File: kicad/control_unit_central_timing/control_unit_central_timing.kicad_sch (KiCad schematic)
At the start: 10 parts

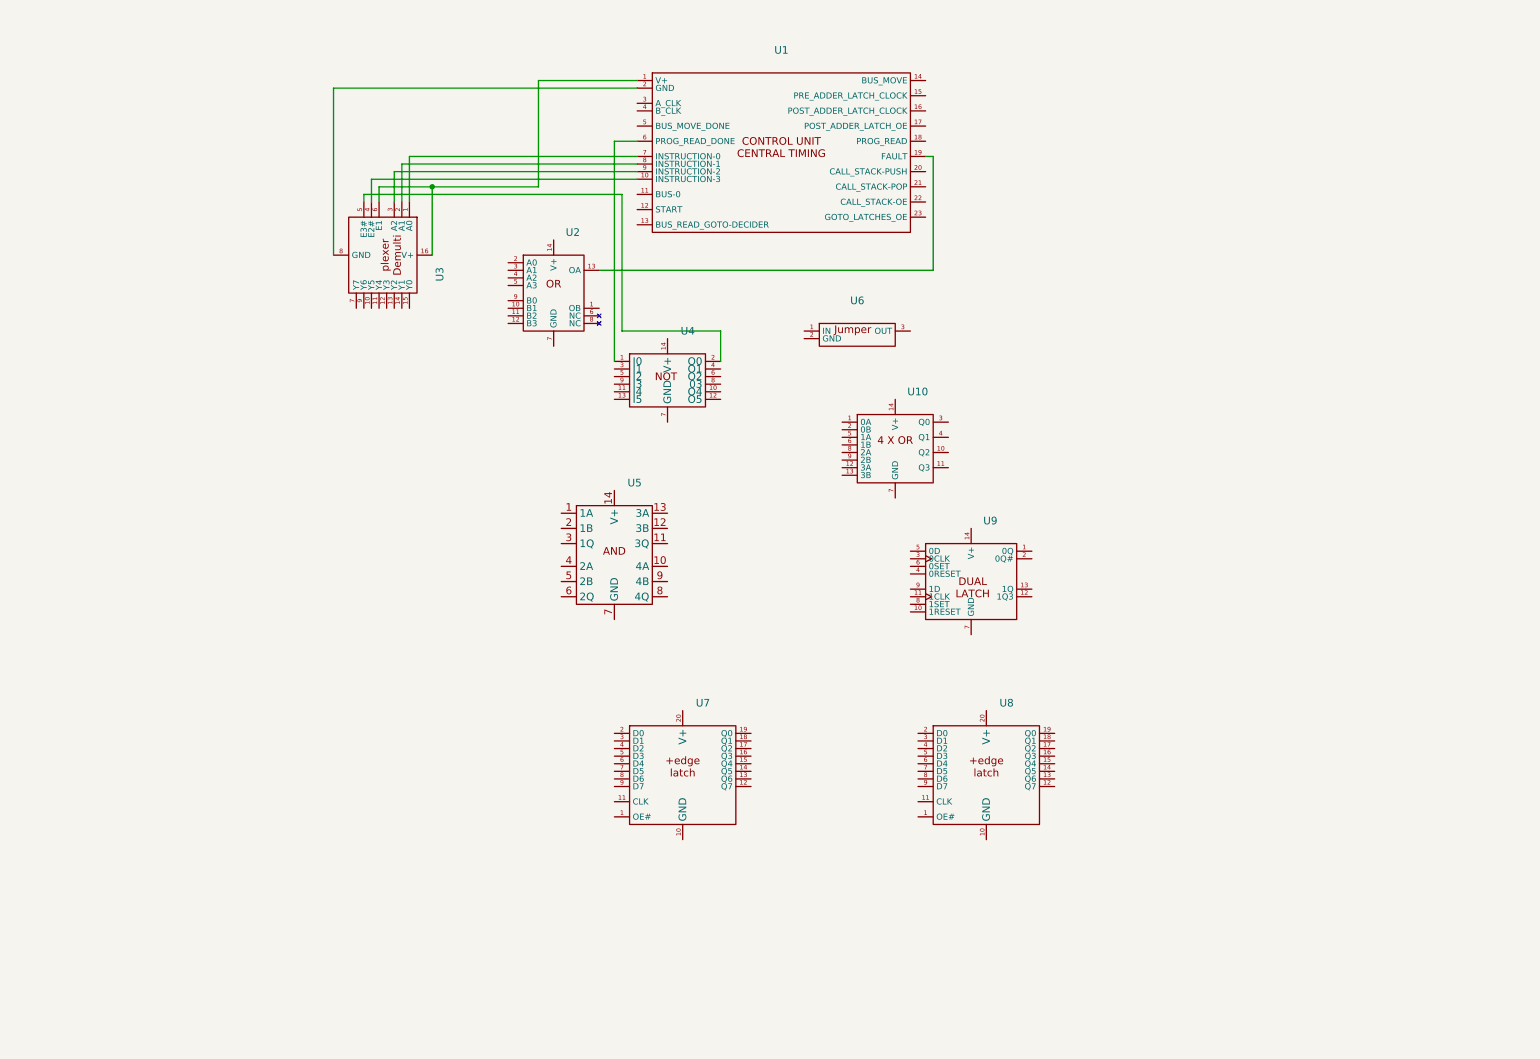
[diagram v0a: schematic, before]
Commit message: Working on control unit schematic
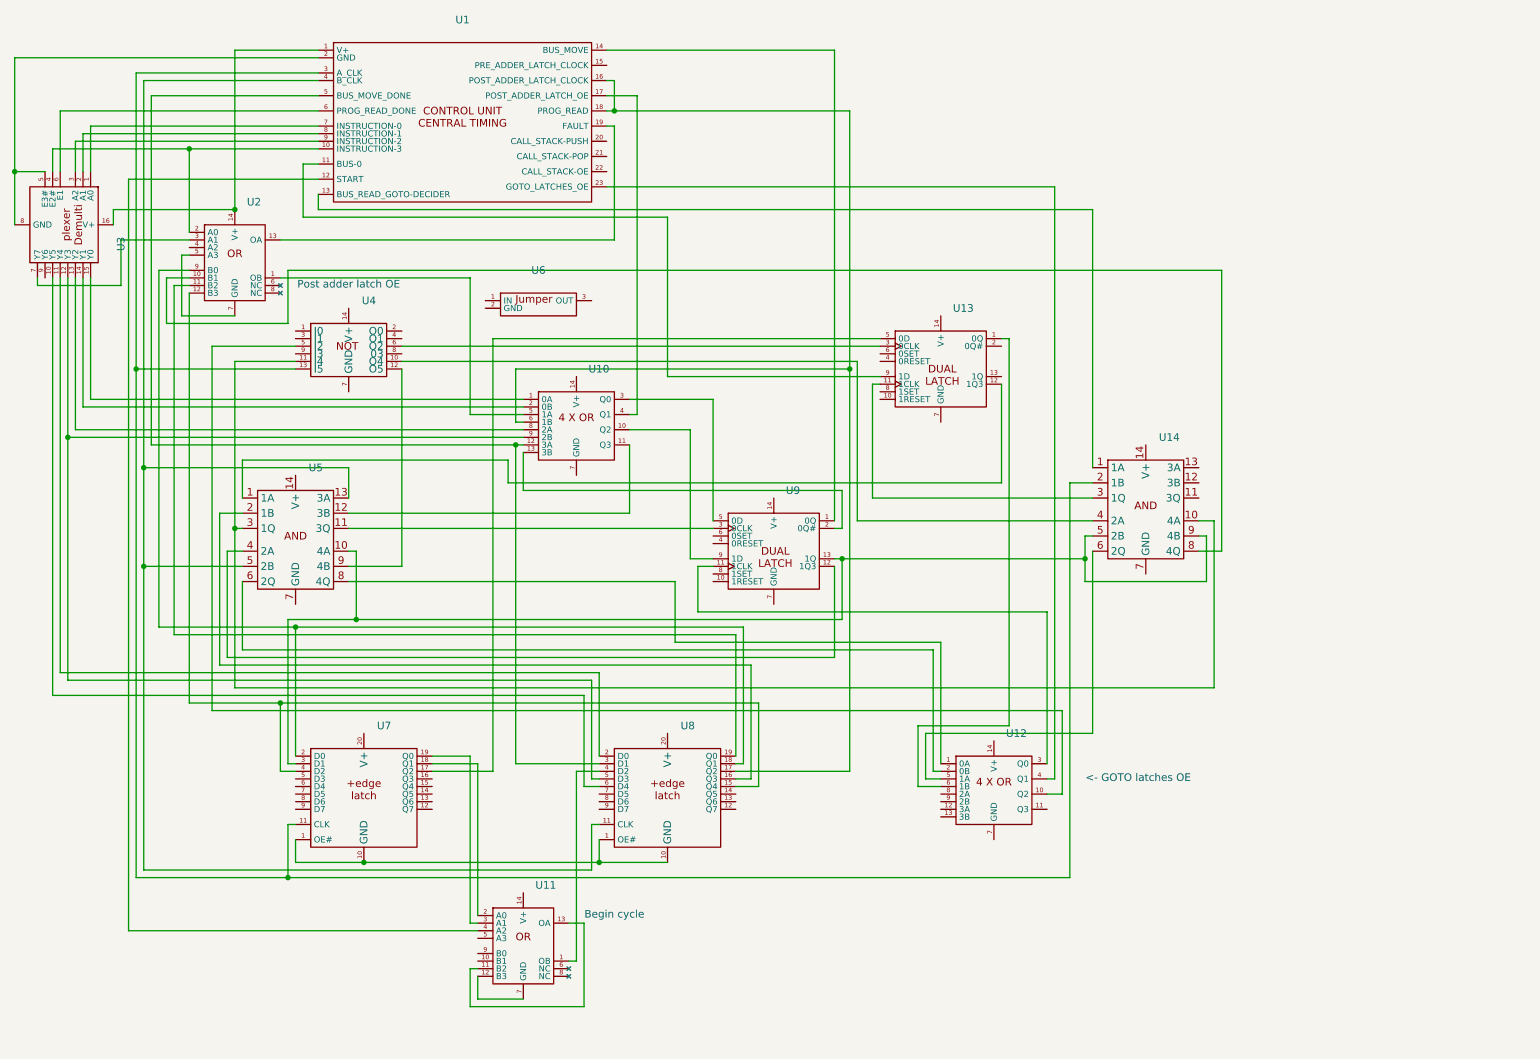
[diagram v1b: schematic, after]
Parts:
- added U11: ~, Package_DIP:DIP-14_W7.62mm, symbol custom_symbol_lib:dual_4_input_OR
- added U12: ~, Package_DIP:DIP-14_W7.62mm, symbol custom_symbol_lib:quad_OR
- added U13: ~, Package_DIP:DIP-14_W7.62mm, symbol custom_symbol_lib:dual_latch
- added U14: ~, Package_DIP:DIP-14_W7.62mm, symbol custom_symbol_lib:quad_and
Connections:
- net at U9.1 (0Q): now also U1.14 (BUS_MOVE)
- net at U9.11 (1CLK): now also U12.3 (Q0)
- net at U9.12 (1Q3): now also U5.4 (2A)
- net at U9.13 (1Q): now also U5.10 (4A), U7.3 (D1), U14.5 (2B), U14.9 (4B)
- net at U9.2 (0Q#): now also U10.13 (3B)
- net at U9.3 (0CLK): now also U5.11 (3Q)
- net at U9.5 (0D): now also U10.3 (Q0)
- net at U9.9 (1D): now also U10.10 (Q2)
- net at U8.1 (OE#): now also U7.1 (OE#), U7.10 (GND), U8.10 (GND)
- net at U8.11 (CLK): now also U1.4 (B_CLK), U5.13 (3A), U5.5 (2B)
- net at U8.15 (Q4): now also U2.12 (B3), U7.4 (D2)
- net at U8.16 (Q3): now also U5.2 (1B)
- net at U8.17 (Q2): now also U1.16 (POST_ADDER_LATCH_CLOCK), U1.18 (PROG_READ), U10.6 (1B)
- net at U8.18 (Q1): now also U2.9 (B0), U7.2 (D0)
- net at U8.19 (Q0): now also U2.11 (B2)
- net at U8.2 (D0): now also U3.11 (Y4)
- net at U8.3 (D1): now also U1.5 (BUS_MOVE_DONE), U10.12 (3A)
- net at U8.4 (D2): now also U11.1 (OB)
- net at U8.5 (D3): now also U10.9 (2B), U3.12 (Y3)
- net at U8.6 (D4): now also U3.10 (Y5)
- net at U5.1 (1A): now also U13.12 (1Q3)
- net at U5.12 (3B): now also U10.11 (Q3)
- net at U5.3 (1Q): now also U4.11 (I4), U14.10 (4A)
- net at U5.6 (2Q): now also U12.2 (0B)
- net at U5.8 (4Q): now also U12.1 (0A)
- net at U5.9 (4B): now also U4.12 (O5)
- net at U7.11 (CLK): now also U1.3 (A_CLK), U4.13 (I5), U14.2 (1B)
- net at U7.17 (Q2): now also U13.5 (0D)
- net at U7.18 (Q1): now also U11.2 (A0)
- net at U7.19 (Q0): now also U11.3 (A1)
- net at U1.1 (V+), U3.16 (V+): now also U2.14 (V+); no longer U3.6 (E1)
- net at U1.10 (INSTRUCTION-3), U3.4 (E2#): now also U2.2 (A0)
- net at U1.11 (BUS-0): now also U13.9 (1D)
- net at U1.12 (START): now also U11.4 (A2)
- net at U1.13 (BUS_READ_GOTO-DECIDER): now also U14.1 (1A)
- net at U1.17 (POST_ADDER_LATCH_OE): now also U10.4 (Q1)
- net at U1.2 (GND), U3.8 (GND): now also U3.5 (E3#)
- net at U1.23 (GOTO_LATCHES_OE): now also U12.4 (Q1)
- net at U1.6 (PROG_READ_DONE): now also U3.6 (E1); no longer U4.1 (I0)
- net at U3.13 (Y2): now also U10.8 (2A)
- net at U3.14 (Y1): now also U10.2 (0B)
- net at U3.15 (Y0): now also U10.1 (0A)
- net at U4.2 (O0): no longer U3.5 (E3#)
- net at U3.7 (Y7): now also U2.3 (A1)
- net at U10.5 (1A): now also U2.1 (OB)
- net at U4.10 (O4): now also U14.4 (2A)
- net at U4.5 (I2): now also U12.10 (Q2)
- net at U4.6 (O2): now also U13.3 (0CLK)
- net at U2.10 (B1): now also U14.8 (4Q)
- net at U2.5 (A3): now also U2.7 (GND)
- new net: U12.6 (1B), U13.1 (0Q)
- new net: U13.11 (1CLK), U14.3 (1Q)
- new net: U12.5 (1A), U14.6 (2Q)
- new net: U11.11 (B2), U11.13 (OA)
- new net: U11.12 (B3), U11.7 (GND)
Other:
- note added: "<- GOTO latches OE"
- note added: "Begin cycle"
- note added: "Post adder latch OE"
- moved on the sheet: U1, U10, U2, U3, U4, U5, U6, U7, U8, U9

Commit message: Finished central timing schematic & created progress table
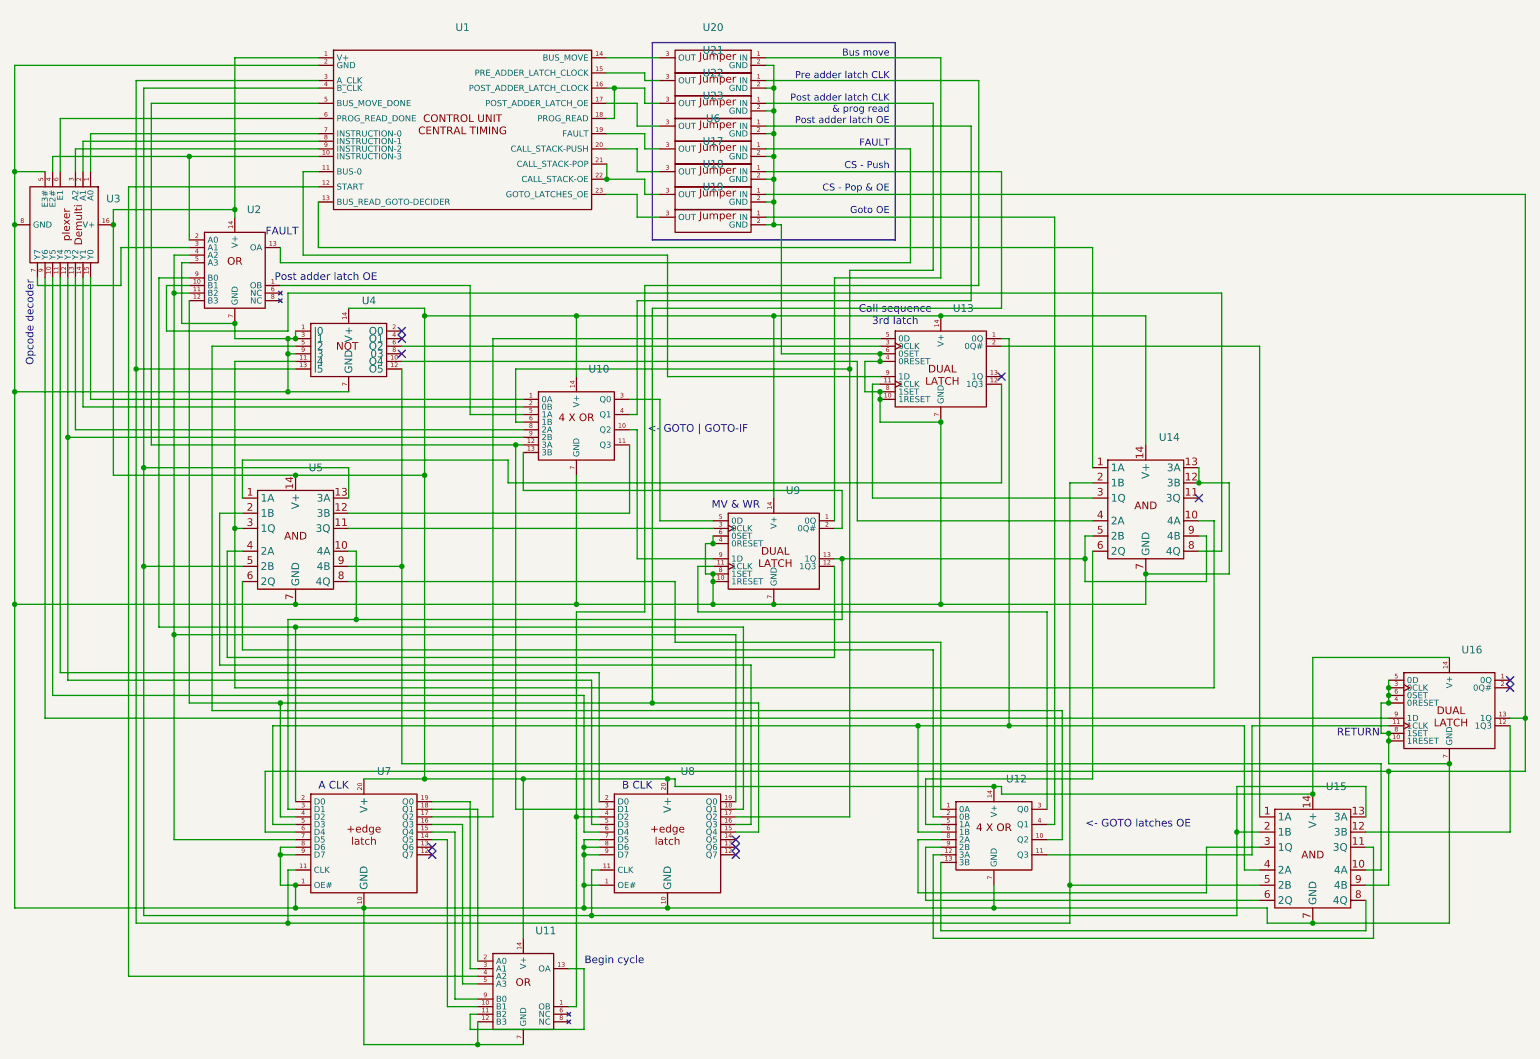
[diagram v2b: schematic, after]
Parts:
- added U15: ~, Package_DIP:DIP-14_W7.62mm, symbol custom_symbol_lib:quad_and
- added U16: ~, Package_DIP:DIP-14_W7.62mm, symbol custom_symbol_lib:dual_latch
- added U17, U18, U19, U20, U21, U22, U23: ~, custom_footprint_library:jumper, symbol custom_symbol_lib:jumper
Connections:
- net at U12.6 (1B), U13.1 (0Q): now also U7.5 (D3), U15.4 (2A)
- net at U13.10 (1RESET): now also U1.2 (GND), U10.7 (GND), U11.12 (B3), U11.7 (GND), U12.7 (GND), U13.4 (0RESET), U13.6 (0SET), U13.7 (GND), U13.8 (1SET), U14.12 (3B), U14.13 (3A), U14.7 (GND), U2.5 (A3), U2.7 (GND), U3.5 (E3#), U3.8 (GND), U4.1 (I0), U4.3 (I1), U4.7 (GND), U4.9 (I3), U5.7 (GND), U6.2 (GND), U7.1 (OE#), U7.10 (GND), U7.8 (D6), U7.9 (D7), U8.1 (OE#), U8.10 (GND), U8.7 (D5), U8.8 (D6), U8.9 (D7), U9.10 (1RESET), U9.4 (0RESET), U9.6 (0SET), U9.7 (GND), U9.8 (1SET), U15.7 (GND), U16.10 (1RESET), U16.3 (0CLK), U16.4 (0RESET), U16.5 (0D), U16.6 (0SET), U16.7 (GND), U16.8 (1SET), U17.2 (GND), U18.2 (GND), U19.2 (GND), U20.2 (GND), U21.2 (GND), U22.2 (GND), U23.2 (GND)
- net at U13.14 (V+): now also U1.1 (V+), U10.14 (V+), U11.14 (V+), U12.14 (V+), U14.14 (V+), U2.14 (V+), U3.16 (V+), U4.14 (V+), U5.14 (V+), U7.20 (V+), U8.20 (V+), U9.14 (V+), U15.14 (V+), U16.14 (V+)
- net at U13.2 (0Q#): now also U15.1 (1A)
- net at U6.1 (IN): now also U2.13 (OA)
- net at U6.3 (OUT): now also U1.19 (FAULT)
- net at U9.1 (0Q): now also U20.1 (IN); no longer U1.14 (BUS_MOVE)
- net at U1.4 (B_CLK), U5.13 (3A), U5.5 (2B)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: now also U15.13 (3A), U15.2 (1B)
- net at U2.12 (B3), U7.4 (D2), U8.15 (Q4): now also U17.1 (IN)
- net at U10.6 (1B), U8.17 (Q2): now also U22.1 (IN); no longer U1.16 (POST_ADDER_LATCH_CLOCK), U1.18 (PROG_READ)
- net at U2.11 (B2), U8.19 (Q0): now also U2.4 (A2), U7.7 (D5)
- net at U11.1 (OB), U8.4 (D2): now also U21.1 (IN)
- net at U12.11 (Q3): now also U16.11 (1CLK)
- net at U12.12 (3A): now also U15.11 (3Q)
- net at U12.13 (3B): now also U15.8 (4Q)
- net at U12.4 (Q1): now also U19.1 (IN); no longer U1.23 (GOTO_LATCHES_OE)
- net at U12.8 (2A): now also U15.3 (1Q)
- net at U12.9 (2B): now also U15.6 (2Q)
- net at U4.12 (O5), U5.9 (4B): now also U15.10 (4A)
- net at U1.3 (A_CLK), U14.2 (1B), U4.13 (I5)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: now also U15.5 (2B)
- net at U7.14 (Q5): now also U11.10 (B1)
- net at U7.15 (Q4): now also U11.9 (B0)
- net at U7.16 (Q3): now also U11.5 (A3)
- net at U7.6 (D4): now also U15.9 (4B), U16.13 (1Q), U18.1 (IN)
- net at U1.15 (PRE_ADDER_LATCH_CLOCK): now also U21.3 (OUT)
- net at U1.17 (POST_ADDER_LATCH_OE): now also U23.3 (OUT); no longer U10.4 (Q1)
- net at U1.20 (CALL_STACK-PUSH): now also U17.3 (OUT)
- net at U1.21 (CALL_STACK-POP): now also U1.22 (CALL_STACK-OE), U18.3 (OUT)
- net at U3.9 (Y6): now also U16.9 (1D)
- new net: U1.23 (GOTO_LATCHES_OE), U19.3 (OUT)
- new net: U1.14 (BUS_MOVE), U20.3 (OUT)
- new net: U15.12 (3B), U16.12 (1Q3)
- new net: U1.16 (POST_ADDER_LATCH_CLOCK), U1.18 (PROG_READ), U22.3 (OUT)
- new net: U10.4 (Q1), U23.1 (IN)
- no-connect marks 0 -> 12
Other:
- note added: "<- GOTO | GOTO-IF"
- note added: "A CLK"
- note added: "B CLK"
- note added: "Call sequence 3rd latch"
- note added: "FAULT"
- note added: "MV & WR"
- note added: "Opcode decoder"
- note added: "RETURN"
- title: (none) -> Control unit central timing
- moved on the sheet: U1, U11, U12, U2, U7, U8

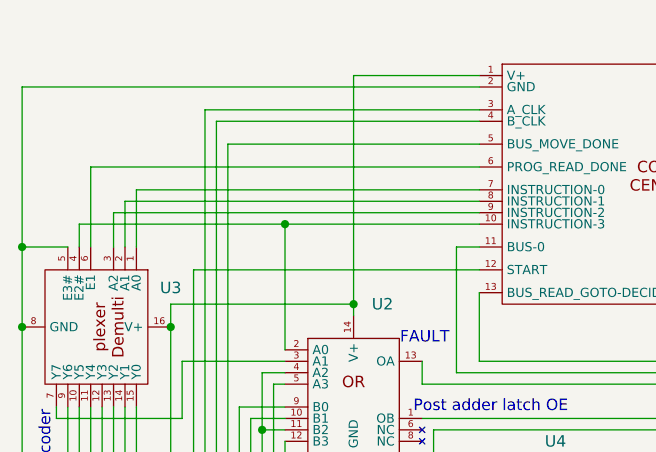
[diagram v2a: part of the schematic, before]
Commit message: Updating parts spreadsheet (not done)
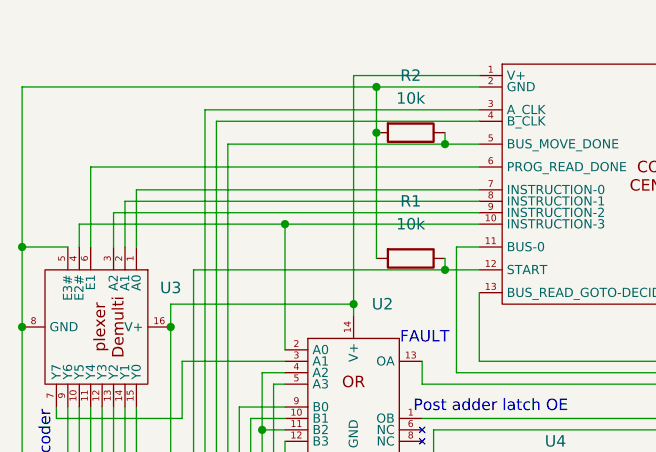
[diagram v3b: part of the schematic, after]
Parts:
- added R1, R2: 10k, custom_footprint_library:0.4_pitch_resistor, symbol Device:R
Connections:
- net at U1.2 (GND), U10.7 (GND), U11.12 (B3)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: now also R1.2, R2.2
- net at U1.5 (BUS_MOVE_DONE), U10.12 (3A), U8.3 (D1): now also R2.1
- net at U1.12 (START), U11.4 (A2): now also R1.1
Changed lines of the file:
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@@
 	)
 	(junction
+		(at 59.69 36.83)
+		(diameter 0)
+		(color 0 0 0 0)
+	)
+	(junction
 		(at 242.57 121.92)
 		(diameter 0)
@@
 	)
 	(junction
+		(at 59.69 22.86)
+		(diameter 0)
+		(color 0 0 0 0)
+	)
+	(junction
 		(at 163.83 127)
 		(diameter 0)
@@
 	)
 	(junction
+		(at 52.07 16.51)
+		(diameter 0)
+		(color 0 0 0 0)
+	)
+	(junction
 		(at 217.17 144.78)
 		(diameter 0)
@@
 	)
 	(junction
+		(at 52.07 21.59)
+		(diameter 0)
+		(color 0 0 0 0)
+	)
+	(junction
 		(at 29.21 43.18)
 		(diameter 0)
@@
 	(wire
 		(pts
+			(xy 59.69 22.86) (xy 35.56 22.86)
+		)
+		(stroke
+			(width 0)
+			(type default)
+		)
+	)
+	(wire
+		(pts
 			(xy 25.4 52.07) (xy 25.4 72.39)
 		)
@@
 	(wire
 		(pts
+			(xy 59.69 35.56) (xy 59.69 36.83)
+		)
+		(stroke
+			(width 0)
+			(type default)
+		)
+	)
+	(wire
+		(pts
 			(xy 212.09 147.32) (xy 212.09 154.94)
 		)
@@
 	(wire
 		(pts
-			(xy 63.5 36.83) (xy 31.75 36.83)
+			(xy 63.5 36.83) (xy 59.69 36.83)
 		)
 		(stroke
@@
 	(wire
 		(pts
+			(xy 52.07 16.51) (xy 52.07 21.59)
+		)
+		(stroke
+			(width 0)
+			(type default)
+		)
+	)
+	(wire
+		(pts
 			(xy 41.91 123.19) (xy 41.91 55.88)
 		)
@@
 	(wire
 		(pts
+			(xy 59.69 21.59) (xy 59.69 22.86)
+		)
+		(stroke
+			(width 0)
+			(type default)
+		)
+	)
+	(wire
+		(pts
 			(xy 58.42 62.23) (xy 49.53 62.23)
 		)
@@
 	(wire
 		(pts
+			(xy 59.69 36.83) (xy 31.75 36.83)
+		)
+		(stroke
+			(width 0)
+			(type default)
+		)
+	)
+	(wire
+		(pts
 			(xy 57.15 49.53) (xy 162.56 49.53)
 		)
@@
 	(wire
 		(pts
-			(xy 63.5 22.86) (xy 35.56 22.86)
+			(xy 63.5 22.86) (xy 59.69 22.86)
 		)
 		(stroke
@@
 	(wire
 		(pts
+			(xy 52.07 16.51) (xy 63.5 16.51)
+		)
+		(stroke
+			(width 0)
+			(type default)
+		)
+	)
+	(wire
+		(pts
 			(xy 46.99 91.44) (xy 50.8 91.44)
 		)
@@
 	(wire
 		(pts
+			(xy 52.07 21.59) (xy 52.07 35.56)
+		)
+		(stroke
+			(width 0)
+			(type default)
+		)
+	)
+	(wire
+		(pts
 			(xy 97.79 135.89) (xy 121.92 135.89)
 		)
@@
 	(wire
 		(pts
-			(xy 12.7 16.51) (xy 63.5 16.51)
+			(xy 12.7 16.51) (xy 52.07 16.51)
 		)
 		(stroke
@@
 	)
 	(symbol
+		(lib_id "Device:R")
+		(at 55.88 21.59 270)
+		(unit 1)
+		(exclude_from_sim no)
+		(in_bom yes)
+		(on_board yes)
+		(dnp no)
+		(fields_autoplaced yes)
+		(property "Reference" "R2"
+			(at 55.88 15.24 90)
+			(effects
+				(font
+					(size 1.27 1.27)
+				)
+			)
+		)
+		(property "Value" "10k"
+			(at 55.88 17.78 90)
+			(effects
+				(font
+					(size 1.27 1.27)
+				)
+			)
+		)
+		(property "Footprint" "custom_footprint_library:0.4_pitch_resistor"
+			(at 55.88 19.812 90)
+			(effects
+				(font
+					(size 1.27 1.27)
+				)
+				(hide yes)
+			)
+		)
+		(property "Datasheet" "~"
+			(at 55.88 21.59 0)
+			(effects
+				(font
+					(size 1.27 1.27)
+				)
+				(hide yes)
+			)
+		)
+		(property "Description" "Resistor"
+			(at 55.88 21.59 0)
+			(effects
+				(font
+					(size 1.27 1.27)
+				)
+				(hide yes)
+			)
+		)
+		(pin "2"
+		)
+		(pin "1"
+		)
+		(instances
+			(project "control_unit_central_timing"
+				(path "/1ab0fbc3-d407-418e-ae93-04453340c21e"
+					(reference "R2")
+					(unit 1)
+				)
+			)
+		)
+	)
+	(symbol
 		(lib_id "custom_symbol_lib:jumper")
 		(at 129.54 30.48 0)
@@
 					(unit 1)
 				)
+			)
+		)
+	)
+	(symbol
+		(lib_id "Device:R")
+		(at 55.88 35.56 270)
+		(unit 1)
+		(exclude_from_sim no)
+		(in_bom yes)
+		(on_board yes)
+		(dnp no)
+		(fields_autoplaced yes)
+		(property "Reference" "R1"
+			(at 55.88 29.21 90)
+			(effects
+				(font
+					(size 1.27 1.27)
+				)
+			)
+		)
+		(property "Value" "10k"
+			(at 55.88 31.75 90)
+			(effects
+				(font
+					(size 1.27 1.27)
+				)
+			)
+		)
+		(property "Footprint" "custom_footprint_library:0.4_pitch_resistor"
+			(at 55.88 33.782 90)
+			(effects
+				(font
+					(size 1.27 1.27)
+				)
+				(hide yes)
+			)
+		)
+		(property "Datasheet" "~"
+			(at 55.88 35.56 0)
+			(effects
+				(font
+					(size 1.27 1.27)
+				)
+				(hide yes)
+			)
+		)
+		(property "Description" "Resistor"
+			(at 55.88 35.56 0)
+			(effects
+				(font
+					(size 1.27 1.27)
+				)
+				(hide yes)
+			)
+		)
+		(pin "2"
+		)
+		(pin "1"
+		)
+		(instances
+			(project "control_unit_central_timing"
+				(path "/1ab0fbc3-d407-418e-ae93-04453340c21e"
+					(reference "R1")
+					(unit 1)
+				)
